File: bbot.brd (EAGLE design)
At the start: 64.5 x 53.3 mm, 19 parts

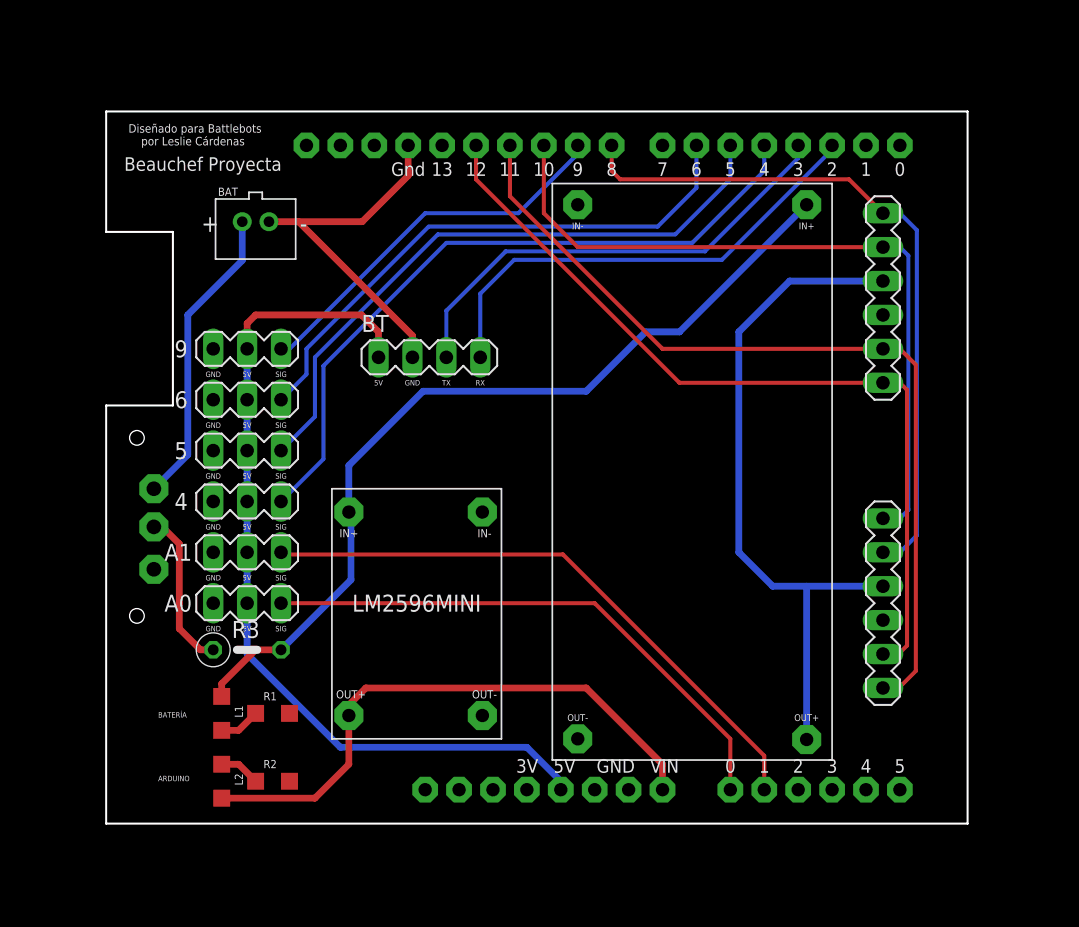
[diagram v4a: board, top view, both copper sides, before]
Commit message: added bp logo, ready to manufacture
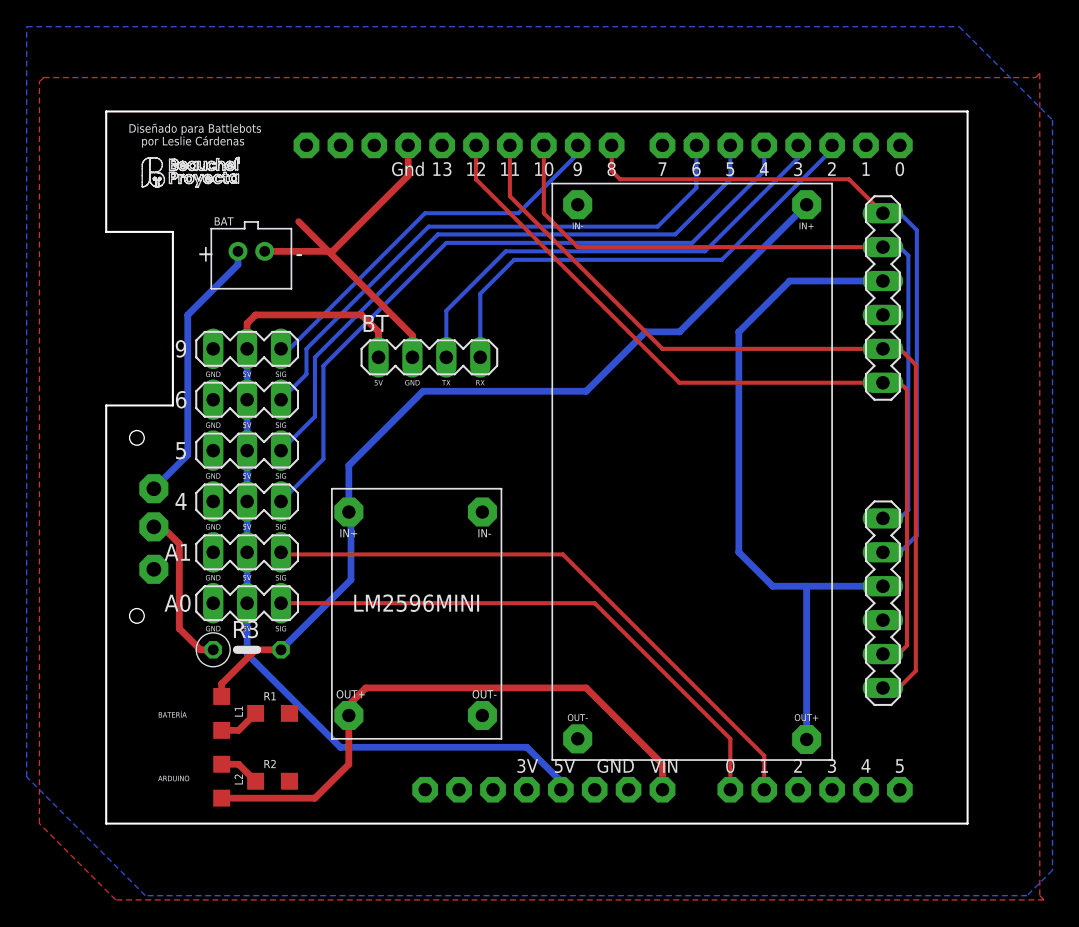
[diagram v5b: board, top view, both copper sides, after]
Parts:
- moved BAT 2.25 mm to (-19.4, 16.2)
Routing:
- net N$7: track 22.7 -> 20.4 mm
- net GND: track 27.8 -> 29.1 mm
- added copper zone on layer 1, net GND
- added copper zone on layer 16, net GND
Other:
- board text removed: "Beauchef Proyecta"
